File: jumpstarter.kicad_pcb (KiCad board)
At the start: 4 copper layers, 170 x 170 mm, 133 parts, among them J1 USB_C_Receptacle_PowerOnly_6P, J10 Conn_01x02_Pin, J11 Conn_01x02_Pin, J12 Conn_01x02_Pin, J13 Conn_01x02_Pin, J14 Conn_01x02_Pin, J2 Barrel_Jack_MountingPin, J3 Barrel_Jack_MountingPin, J4 Conn_01x09_Pin, J5 USB_C_Receptacle_PowerOnly_6P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

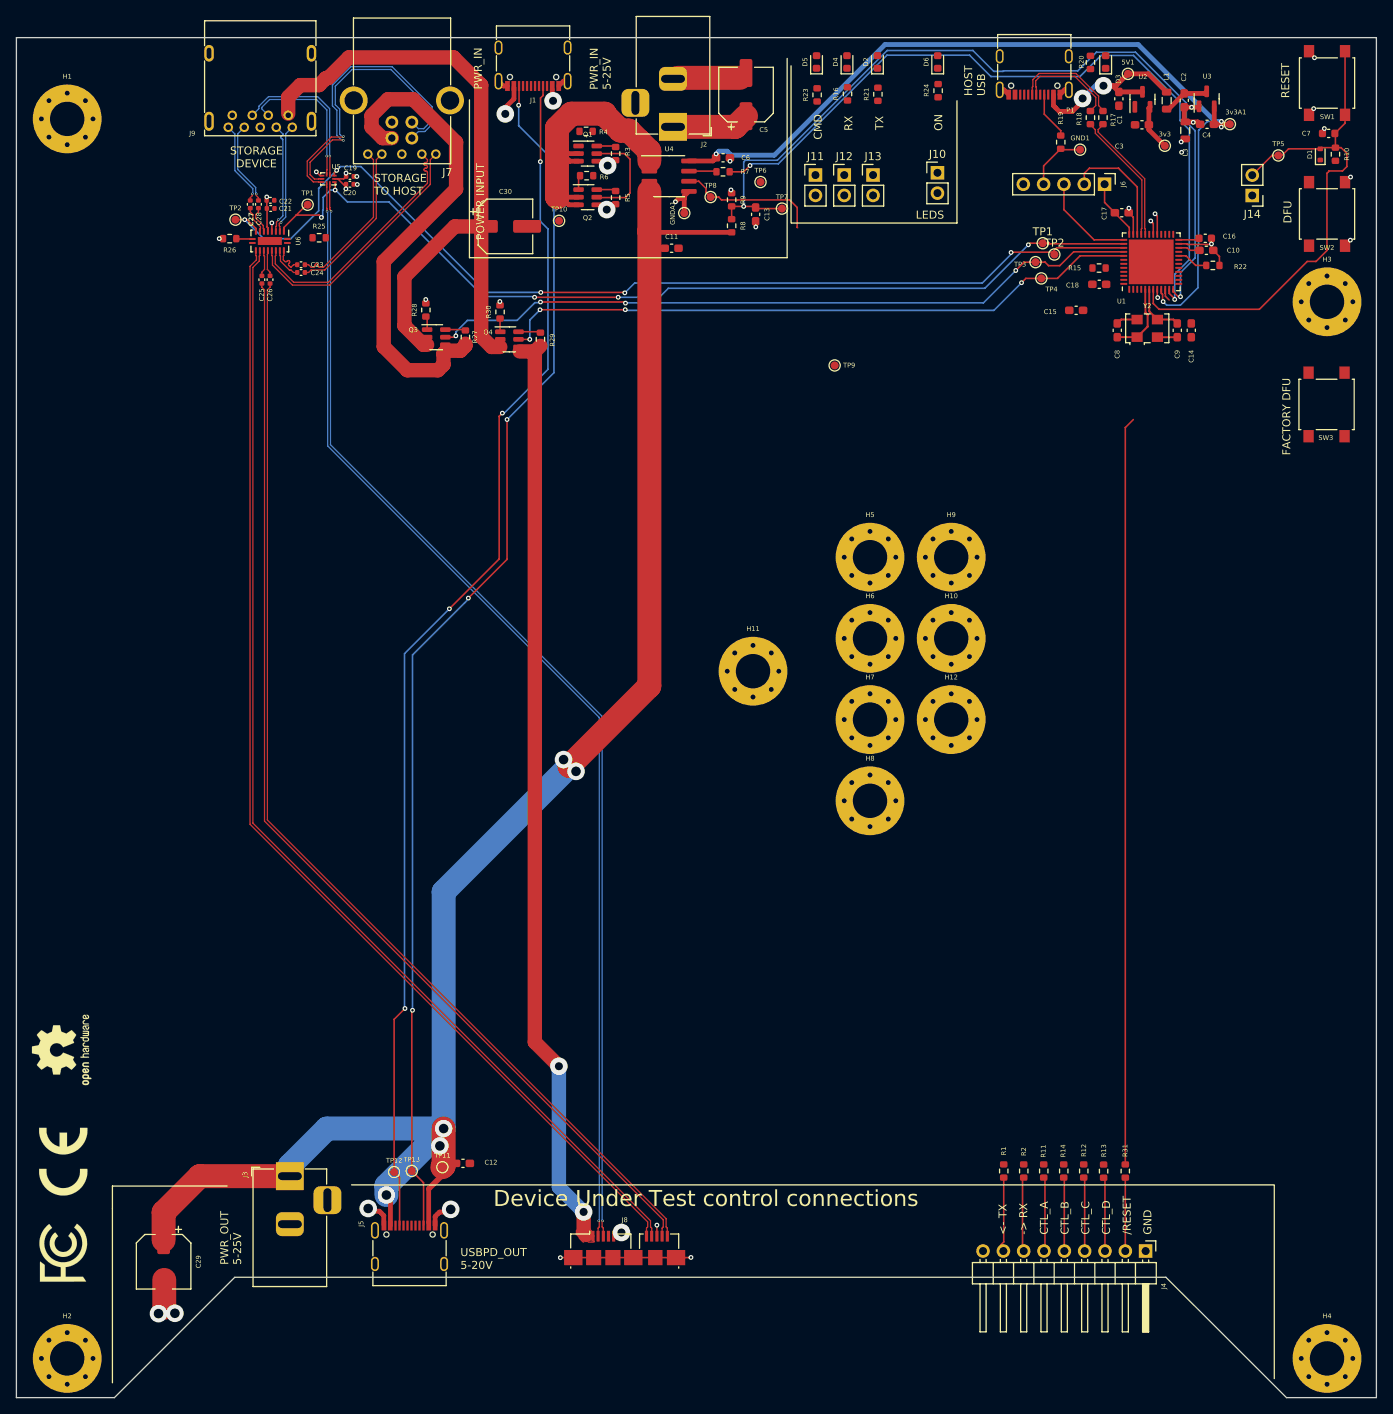
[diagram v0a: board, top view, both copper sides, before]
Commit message: Mounting holes positioned, and routing
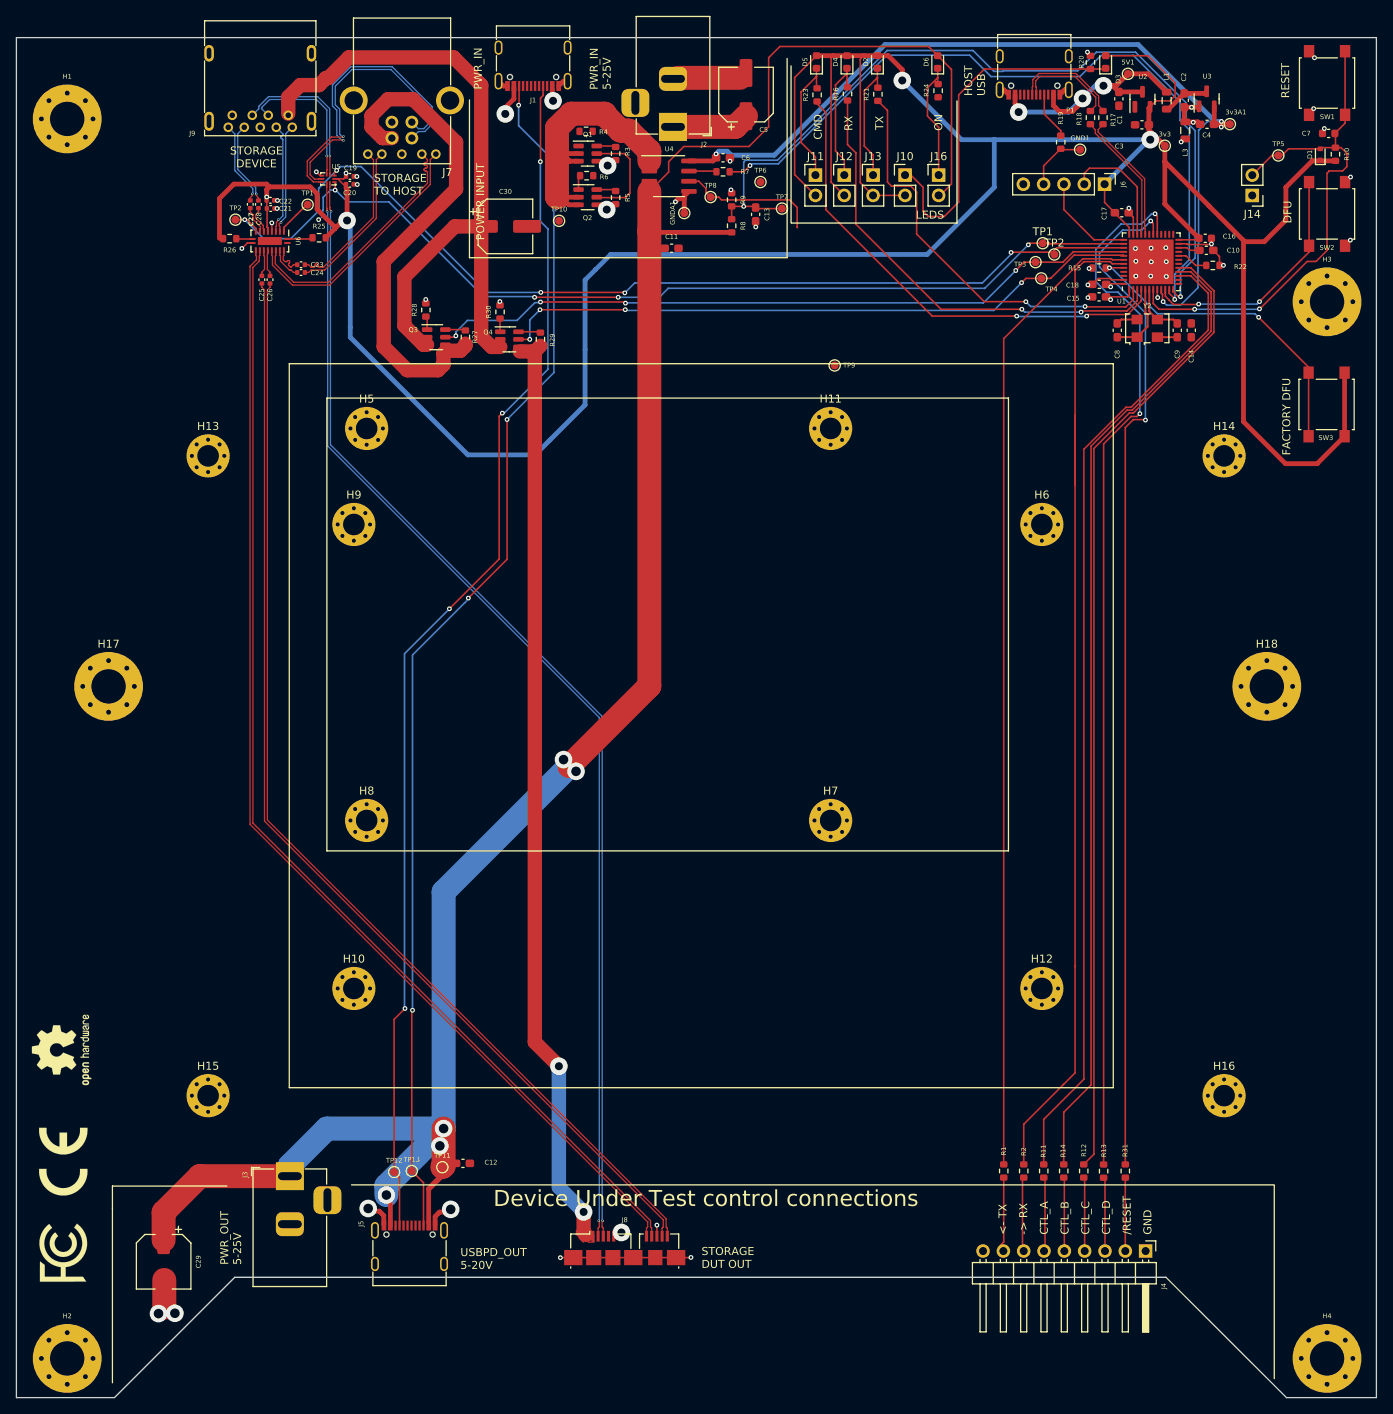
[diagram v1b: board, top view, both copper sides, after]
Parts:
- added H13: Board MountingHole, MountingHole:MountingHole_2.7mm_M2.5_Pad_Via, F.Cu at (81.3, 116.2)
- added H14: Board MountingHole, MountingHole:MountingHole_2.7mm_M2.5_Pad_Via, F.Cu at (208.3, 116.2)
- added H15: Board MountingHole, MountingHole:MountingHole_2.7mm_M2.5_Pad_Via, F.Cu at (81.3, 196.2)
- added H16: Board MountingHole, MountingHole:MountingHole_2.7mm_M2.5_Pad_Via, F.Cu at (208.3, 196.2)
- added H17: ITX MountingHole, MountingHole:MountingHole_4.3mm_M4_Pad_Via, F.Cu at (68.8, 145.0)
- added H18: ITX MountingHole, MountingHole:MountingHole_4.3mm_M4_Pad_Via, F.Cu at (213.6, 145.0)
- added J16: Conn_01x02_Pin, Connector_PinHeader_2.54mm:PinHeader_1x02_P2.54mm_Vertical, F.Cu at (172.6, 81.1)
- H10, H11, H12, H5, H6, H7, H8, H9: footprint MountingHole:MountingHole_4.3mm_M4_Pad_Via -> MountingHole:MountingHole_2.7mm_M2.5_Pad_Via
- moved H10 86.5 mm to (99.5, 182.8)
- moved H9 74.8 mm to (99.5, 124.8)
- moved H5 64.9 mm to (101.1, 112.8)
- moved H8 63.0 mm to (101.1, 161.8)
- moved H12 35.5 mm to (185.5, 182.8)
- moved H11 31.9 mm to (159.1, 112.8)
- moved H6 25.8 mm to (185.5, 124.8)
- moved H7 13.5 mm to (159.1, 161.8)
- moved J10 4.06 mm to (168.4, 81.1)
- moved C15 3.32 mm to (192.7, 96.3)
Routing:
- net +3.3V: track 24.6 -> 416.6 mm, vias 4 -> 7
- net /RX1: track 0.00 -> 129.8 mm
- net /CTL_D: track 2.68 -> 131.8 mm, vias 1 -> 2
- net /TX1: track 0.00 -> 122.5 mm
- net /CTL_A: track 0.00 -> 122.4 mm
- net /CTL_B: track 0.00 -> 122.1 mm
- net /CTL_C: track 0.00 -> 121.8 mm
- net /board_control/VCCOUT: track 209.7 -> 278.5 mm
- net /LED2: track 0.00 -> 61.2 mm, vias 0 -> 2
- net /LED1: track 0.00 -> 57.6 mm, vias 0 -> 2
- net /LED0: track 0.00 -> 52.6 mm, vias 0 -> 2
- net Net-(D3-K): track 0.00 -> 44.5 mm
- net /BOOT0: track 0.00 -> 40.9 mm, vias 0 -> 2
- net /RESET: track 95.3 -> 128.2 mm, vias 1 -> 2
- net /BUTTON: track 1.54 -> 30.7 mm, vias 0 -> 2
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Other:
- board text added: "STORAGE DUT OUT"

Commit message: Update
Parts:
- removed TP8: TestPoint, TestPoint:TestPoint_Pad_D1.0mm
- added C31: 1uF, Capacitor_SMD:C_0603_1608Metric_Pad1.08x0.95mm_HandSolder, F.Cu at (177.3, 206.3)
- added C32: 1nF, Capacitor_SMD:C_0603_1608Metric_Pad1.08x0.95mm_HandSolder, F.Cu at (145.0, 83.3)
- added G***: LOGO, LOGO, F.Cu at (62.7, 176.3)
- added J15: Conn_01x02_Pin, Connector_PinHeader_2.54mm:PinHeader_1x02_P2.54mm_Vertical, F.Cu at (212.6, 91.7)
- added REF**: Symbol_Barrel_Polarity, Symbol:Symbol_Barrel_Polarity, F.Cu at (81.2, 206.1)
- added REF**: WEEE-Logo_5.6x8mm_SilkScreen, Symbol:WEEE-Logo_5.6x8mm_SilkScreen, F.Cu at (221.6, 215.8)
- added REF**: ESD-Logo_8.9x8mm_SilkScreen, Symbol:ESD-Logo_8.9x8mm_SilkScreen, F.Cu at (220.7, 203.7)
- added REF**: Symbol_Barrel_Polarity, Symbol:Symbol_Barrel_Polarity, F.Cu at (148.6, 65.0)
- added TP11: TestPoint, TestPoint:TestPoint_Pad_D1.0mm, F.Cu at (143.4, 88.9)
- H17, H18: value ITX MountingHole -> cable strap hole
- SW1: footprint Button_Switch_SMD:SW_SPST_B3S-1000 -> Button_Switch_THT:SW_Tactile_SPST_Angled_PTS645Vx58-2LFS
- U4: value ACS722xLCTR-20AU -> ACS725LLCTR-05AB-T
- Y2: footprint Oscillator:Oscillator_SMD_EuroQuartz_XO53-4Pin_5.0x3.2mm -> Oscillator:Oscillator_SMD_EuroQuartz_XO32-4Pin_3.2x2.5mm
- moved TP9 12.1 mm to (165.5, 94.4)
- moved C14 7.44 mm to (207.0, 93.6), turned to 0 degrees
- moved TP7 5.41 mm to (148.5, 82.3)
- moved SW1 3.84 mm to (218.3, 67.0), turned to 0 degrees
- moved GNDA1 2.56 mm to (143.3, 85.5)
- moved TP5 1.70 mm to (216.6, 77.9)
- moved J14 1.38 mm to (212.6, 82.6)
- moved U4 1.28 mm to (140.2, 81.3)
- moved TP6 1.28 mm to (150.1, 80.7)
- moved R22 0.38 mm to (206.9, 92.0)
- turned Y2 to 90 degrees
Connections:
- H1 pad 1: (no net) -> GND
- H10 pad 1: (no net) -> GND
- H11 pad 1: (no net) -> GND
- H12 pad 1: (no net) -> GND
- H13 pad 1: (no net) -> GND
- H14 pad 1: (no net) -> GND
- H15 pad 1: (no net) -> GND
- H16 pad 1: (no net) -> GND
- H17 pad 1: (no net) -> GND
- H18 pad 1: (no net) -> GND
- H2 pad 1: (no net) -> GND
- H3 pad 1: (no net) -> GND
- H4 pad 1: (no net) -> GND
- H5 pad 1: (no net) -> GND
- H6 pad 1: (no net) -> GND
- H7 pad 1: (no net) -> GND
- H8 pad 1: (no net) -> GND
- H9 pad 1: (no net) -> GND
- J4 pad 9: /board_control/V_IO -> +3.3V
- J6 pad 5: unconnected-(J6-Pin_5-Pad5) -> /NRST
- U1 pad 13: /BW_SEL -> unconnected-(U1-PA3-Pad13)
- U4 pad 1: /board_control/VCCOUT_SW -> /board_control/VCCOUT
- U4 pad 2: /board_control/VCCOUT_SW -> /board_control/VCCOUT
- U4 pad 3: /board_control/VCCOUT -> /board_control/VCCOUT_SW
- U4 pad 4: /board_control/VCCOUT -> /board_control/VCCOUT_SW
- U4 pad 6: /BW_SEL -> Net-(U4-BW_SEL)
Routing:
- net +3.3V: track 416.6 -> 567.5 mm, vias 7 -> 5
- net /ON_OFF: track 13.1 -> 109.3 mm, vias 0 -> 4
- net /NRST: track 67.2 -> 107.9 mm, vias 2 -> 3
- net /BW_SEL: track 17.7 -> 0.00 mm
- net /board_control/VCCOUT_SW: track 32.0 -> 43.0 mm
- net GND: track 76.3 -> 86.6 mm, vias 40 -> 60
- net /RX1: track 129.8 -> 121.1 mm
- net /board_control/VCCOUT: track 278.5 -> 284.2 mm, vias 5 -> 7
- net +3.3VA: track 110.6 -> 113.9 mm
- net /CTL_D: track 131.8 -> 128.5 mm
- net /BUTTON: track 30.7 -> 33.5 mm
- net +5V: track 35.0 -> 32.5 mm
- net Net-(U4-BW_SEL): track 0.00 -> 2.52 mm
- net /RESET: track 128.2 -> 125.8 mm
- net /USB_OEn: track 117.1 -> 119.1 mm
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- added copper zone on In1.Cu, net GND
- added copper zone on In2.Cu, net GND
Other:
- board text added: "+"
- board text added: "-"
- board text added: "3.3V I/O pins only"
- board text added: "3v3"
- board text added: "BUTTON"
- board text added: "DUT_ON"
- board text added: "Mini ITX form factor"
- board text added: "POWER"
- board text added: "REL 1.0.0"
- board text added: "SWCLK"
- board text added: "SWD DEBUG"
- board text added: "SWDIO"
- board text added: "V IO"
- board text added: "do not connect V/IO to device under test, only provided to enable voltage translation boards."
- board text added: "github.com/redhat-et/jumpstarter"
- board text removed: "ON"
